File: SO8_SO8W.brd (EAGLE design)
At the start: 13 parts

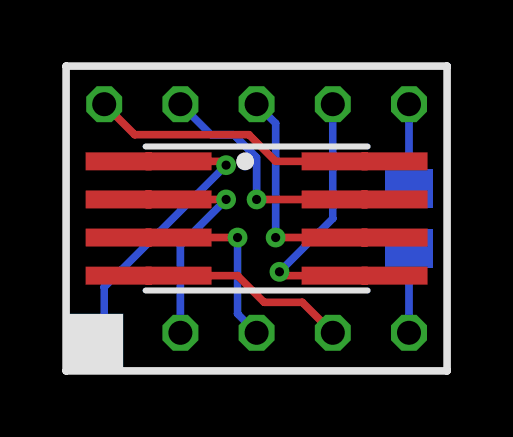
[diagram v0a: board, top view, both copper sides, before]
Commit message: adjusted trace widths
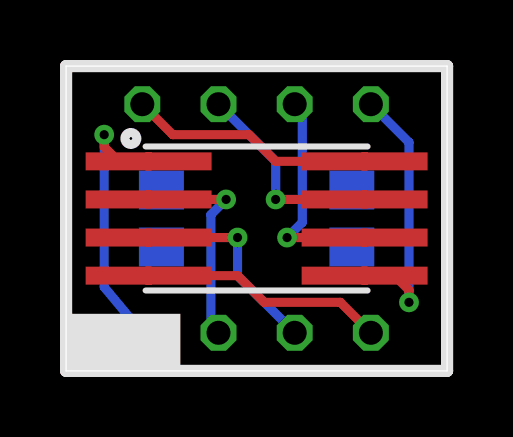
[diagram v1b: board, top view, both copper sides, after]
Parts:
- removed E$129, E$130, E$83, E$84, E$85, E$86, E$87, E$88, E$89, E$90: (no value), drill:1
- removed E$135: (no value), ref-packages:C0805K
- added E$1, E$2: (no value), ref-packages:C0805
- added E$636, E$637, E$638, E$639, E$640, E$641, E$642, E$643: (no value), drill:1
- turned E$635 to 270 degrees
- turned E$644 to 270 degrees
- renumbered E$634 to E$644, E$67 to E$635
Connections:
- removed net S$43: E$635.1, E$644.1, E$87.P$1
- removed net S$44: E$635.2, E$644.2, E$88.P$1
- removed net S$45: E$635.3, E$644.3, E$89.P$1
- removed net S$46: E$635.4, E$644.4, E$90.P$1
- removed net S$47: E$635.8, E$644.8, E$83.P$1
- removed net S$48: E$635.7, E$644.7, E$84.P$1
- removed net S$49: E$635.6, E$644.6, E$85.P$1
- removed net S$50: E$635.5, E$644.5, E$86.P$1
- removed net S$83: E$130.P$1, E$135.1
- removed net S$85: E$129.P$1, E$135.2
- new net S$309: E$635.1, E$640.P$1, E$644.1
- new net S$310: E$635.2, E$641.P$1, E$644.2
- new net S$311: E$635.3, E$642.P$1, E$644.3
- new net S$312: E$635.4, E$643.P$1, E$644.4
- new net S$313: E$635.8, E$636.P$1, E$644.8
- new net S$314: E$635.7, E$637.P$1, E$644.7
- new net S$315: E$635.6, E$638.P$1, E$644.6
- new net S$316: E$635.5, E$639.P$1, E$644.5
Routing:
- net S$50: track 12.9 -> 0.00 mm, vias 1 -> 0
- net S$313: track 0.00 -> 11.2 mm
- net S$46: track 10.5 -> 0.00 mm
- net S$316: track 0.00 -> 10.2 mm, vias 0 -> 1
- net S$43: track 10.2 -> 0.00 mm, vias 1 -> 0
- net S$309: track 0.00 -> 10.2 mm, vias 0 -> 1
- net S$47: track 9.93 -> 0.00 mm
- net S$45: track 9.27 -> 0.00 mm, vias 1 -> 0
- net S$312: track 0.00 -> 9.20 mm
- net S$44: track 8.67 -> 0.00 mm, vias 1 -> 0
- net S$49: track 8.66 -> 0.00 mm, vias 1 -> 0
- net S$315: track 0.00 -> 8.34 mm, vias 0 -> 1
- net S$310: track 0.00 -> 8.34 mm, vias 0 -> 1
- net S$311: track 0.00 -> 7.93 mm, vias 0 -> 1
- net S$314: track 0.00 -> 7.93 mm, vias 0 -> 1
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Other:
- board outline added: 12.7 x 10.2 mm
- board text added: "SO8W"
